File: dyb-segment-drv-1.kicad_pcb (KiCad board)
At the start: 2 copper layers, 10 x 3 mm, 183 parts, among them J1 Conn_01x10, Q1 HL2300, Q10 HL2300, Q11 HL2300, Q12 HL2300, Q13 HL2300, Q14 HL2300, Q15 HL2300, Q16 HL2300, Q2 HL2300, Q3 HL2300, Q4 HL2300, Q5 HL2300, Q6 HL2300, Q7 HL2300, Q8 HL2300, Q9 HL2300, SW1 SW_SPDT, U1 AP2112K-1.8, U10 74AUC2G32, U11 74AUC2G32, U12 74AUC2G32, U13 74AUC2G32, U14 74AUC2G32, U15 Inverter_Schmitt_Dual, U16 Inverter_Schmitt_Dual, U17 SN74AUP2G08, U18 SN74AUP2G08, U19 SN74AUP2G08, U2 GS3911AG, U20 SN74AUP2G08, U21 SN74AUP2G08, U22 74AUC2G32, U23 74AUC2G32, U24 74AUC2G32, U25 74AUC2G32, U26 74AUC2G32, U27 GS3911AG, U28 SN74AUP2G08, U29 SN74AUP2G08, U3 SN74AUP2G08, U30 SN74AUP2G08, U31 SN74AUP2G08, U32 SN74AUP2G08, U33 SN74AUP2G08, U34 74AUC2G32, U35 74AUC2G32, U36 74AUC2G32, U37 74AUC2G32, U38 74AUC2G32, U39 74AUC2G32, U4 SN74AUP2G08, U40 Inverter_Schmitt_Dual, U41 Inverter_Schmitt_Dual, U42 SN74AUP2G08, U43 SN74AUP2G08, U44 SN74AUP2G08, U45 SN74AUP2G08, U46 SN74AUP2G08, U47 74AUC2G32, U48 74AUC2G32, U49 74AUC2G32, U5 SN74AUP2G08, U50 74AUC2G32, U51 74AUC2G32, U6 SN74AUP2G08, U7 SN74AUP2G08, U8 SN74AUP2G08, U9 74AUC2G32

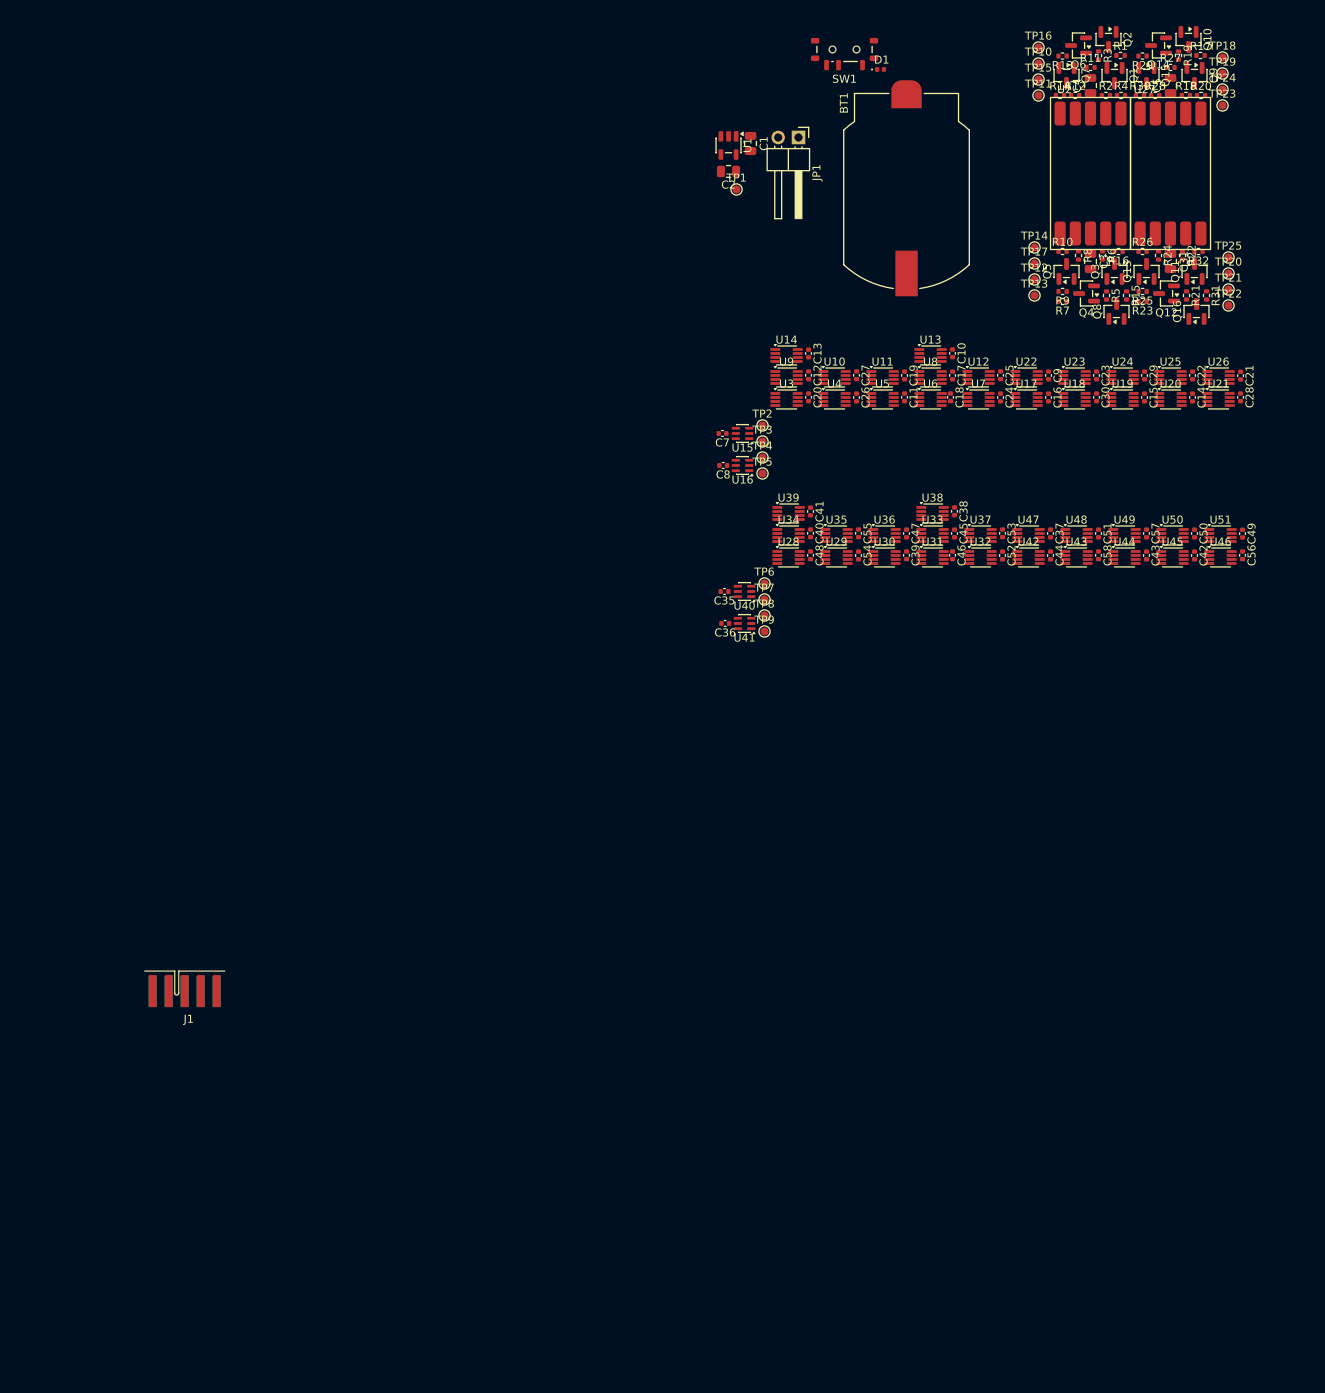
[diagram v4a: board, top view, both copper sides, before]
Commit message: pcb: add initial led driver routing
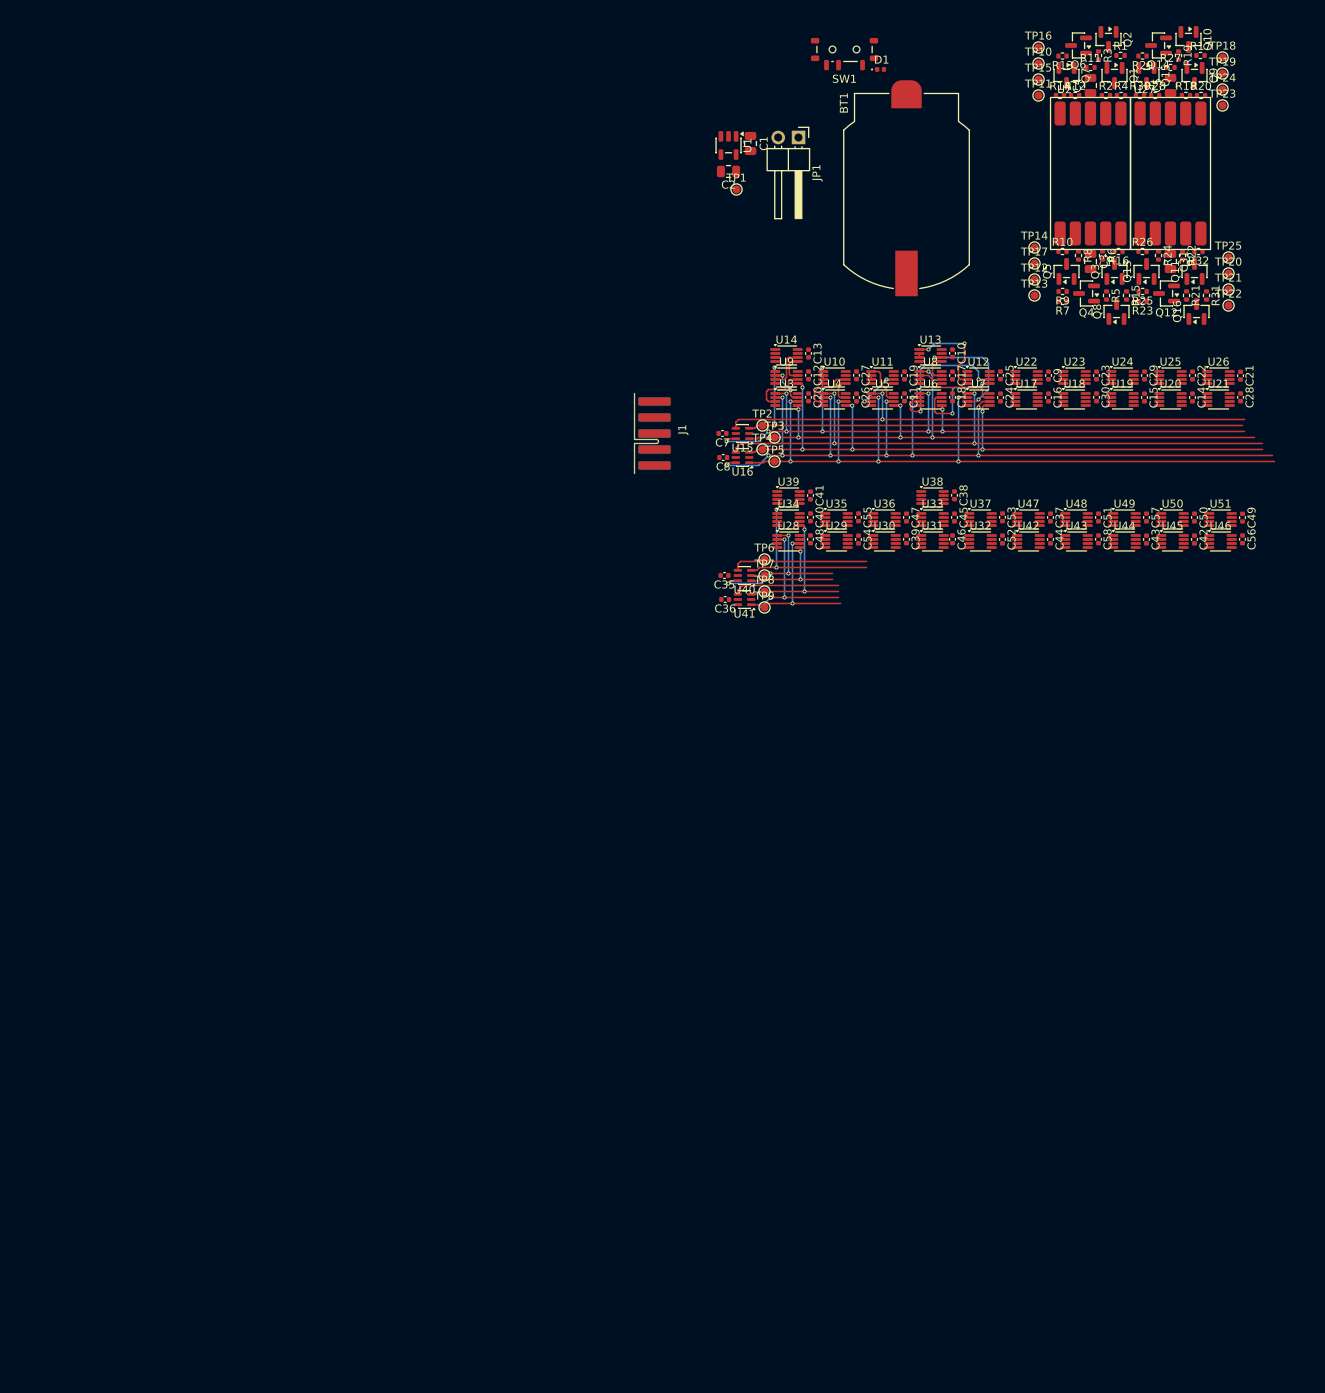
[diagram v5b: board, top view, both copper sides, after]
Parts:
- moved J1 88.1 mm to (101.8, 68.0), turned to 90 degrees
- moved C36 3.00 mm to (113.1, 91.8)
- moved TP6 3.00 mm to (118.0, 86.8)
- moved TP7 3.00 mm to (118.0, 88.8)
- moved TP8 3.00 mm to (118.0, 90.8)
- moved TP9 3.00 mm to (118.0, 92.8)
- moved U41 3.00 mm to (115.5, 91.8)
- moved TP5 2.12 mm to (119.2, 74.5)
- moved C35 2.00 mm to (113.0, 88.8)
- moved C37 2.00 mm to (153.8, 81.5)
- moved C38 2.00 mm to (141.8, 78.7)
- moved C39 2.00 mm to (135.8, 84.2)
- moved C40 2.00 mm to (123.8, 81.5)
- moved C41 2.00 mm to (123.8, 78.8)
- moved C42 2.00 mm to (171.8, 84.2)
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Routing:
- net /Segment Driver/~{D3}: track 0.00 -> 110.0 mm, vias 0 -> 12
- net /A3: track 0.00 -> 100.5 mm, vias 0 -> 8
- net /Segment Driver/~{D1}: track 0.00 -> 90.5 mm, vias 0 -> 10
- net /A2: track 0.00 -> 85.7 mm, vias 0 -> 6
- net /A1: track 0.00 -> 81.7 mm, vias 0 -> 6
- net /Segment Driver/~{D2}: track 0.00 -> 81.4 mm, vias 0 -> 4
- net /A0: track 0.00 -> 69.6 mm, vias 0 -> 2
- net /Segment Driver/~{D0}: track 0.00 -> 69.1 mm, vias 0 -> 2
- net /B0: track 0.00 -> 22.3 mm, vias 0 -> 2
- net /Segment Driver1/~{D1}: track 0.00 -> 21.0 mm, vias 0 -> 4
- net /B2: track 0.00 -> 19.8 mm, vias 0 -> 2
- net /B3: track 0.00 -> 19.6 mm, vias 0 -> 2
- net Net-(U12-Pad6): track 0.00 -> 18.7 mm, vias 0 -> 2
- net /Segment Driver1/~{D3}: track 0.00 -> 18.4 mm, vias 0 -> 3
- net /Segment Driver1/~{D0}: track 0.00 -> 17.0 mm
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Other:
- board size 10 x 3 mm -> 3 x 10 mm

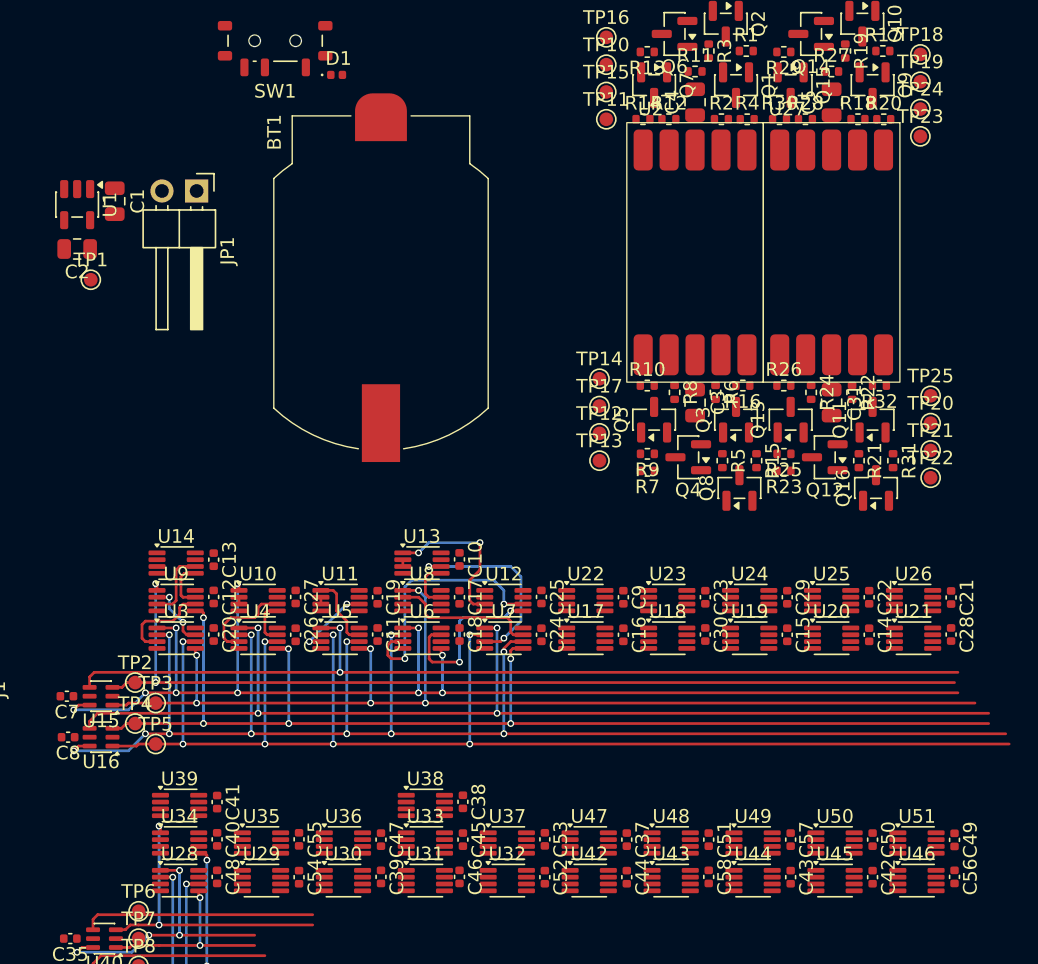
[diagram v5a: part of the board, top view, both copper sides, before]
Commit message: pcb: add tooling holes and fiducials
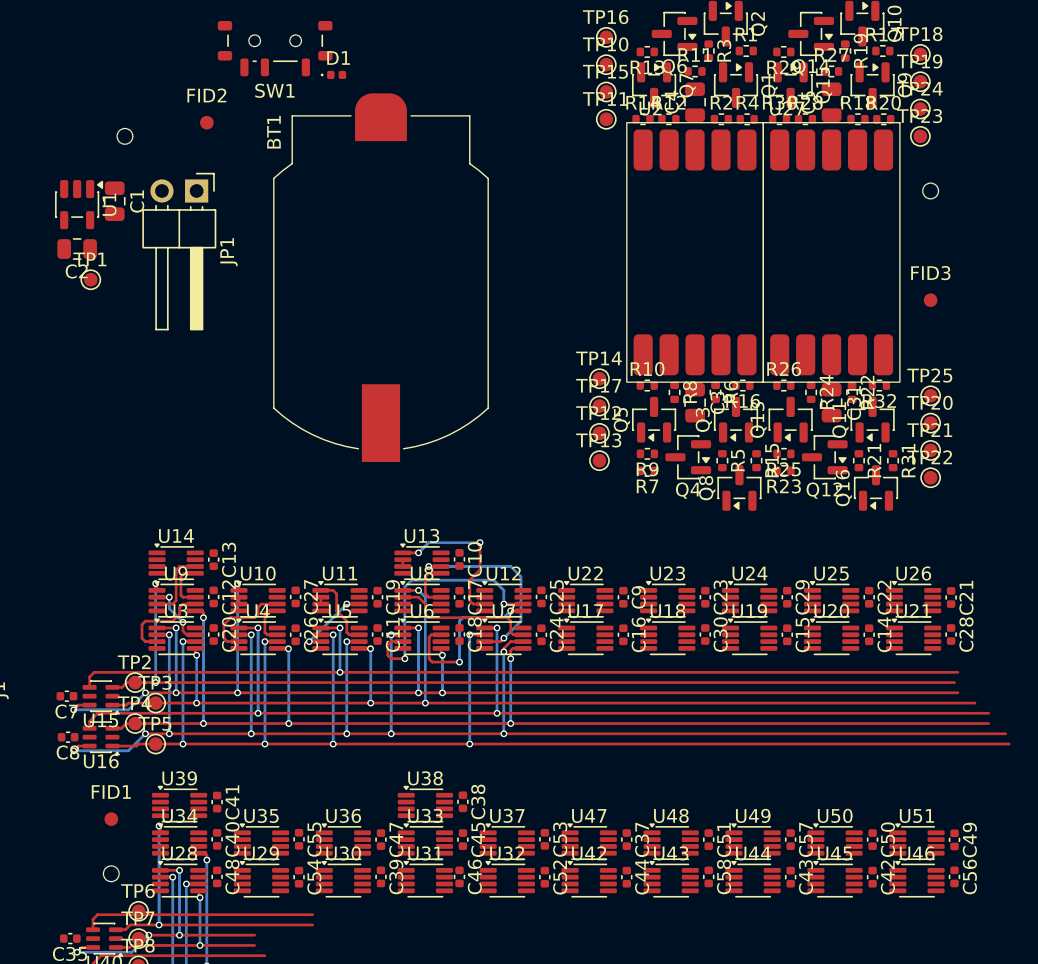
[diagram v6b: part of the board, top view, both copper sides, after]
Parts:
- added FID1: Fiducial, Fiducial:Fiducial_1mm_Mask2mm, F.Cu at (116.0, 80.0)
- added FID2: Fiducial, Fiducial:Fiducial_1mm_Mask2mm, F.Cu at (123.0, 29.0)
- added FID3: Fiducial, Fiducial:Fiducial_1mm_Mask2mm, F.Cu at (176.0, 42.0)
- added H1: MountingHole, MountingHole:ToolingHole_1.152mm, F.Cu at (116.0, 84.0)
- added H2: MountingHole, MountingHole:ToolingHole_1.152mm, F.Cu at (117.0, 30.0)
- added H3: MountingHole, MountingHole:ToolingHole_1.152mm, F.Cu at (176.0, 34.0)

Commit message: pcb: add mounting holes
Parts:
- added H4: MountingHole_Pad, MountingHole:MountingHole_3.2mm_M3_Pad_Via, F.Cu at (115.0, 24.0)
- added H5: MountingHole_Pad, MountingHole:MountingHole_3.2mm_M3_Pad_Via, F.Cu at (181.0, 90.0)
- added H6: MountingHole_Pad, MountingHole:MountingHole_3.2mm_M3_Pad_Via, F.Cu at (181.0, 24.0)

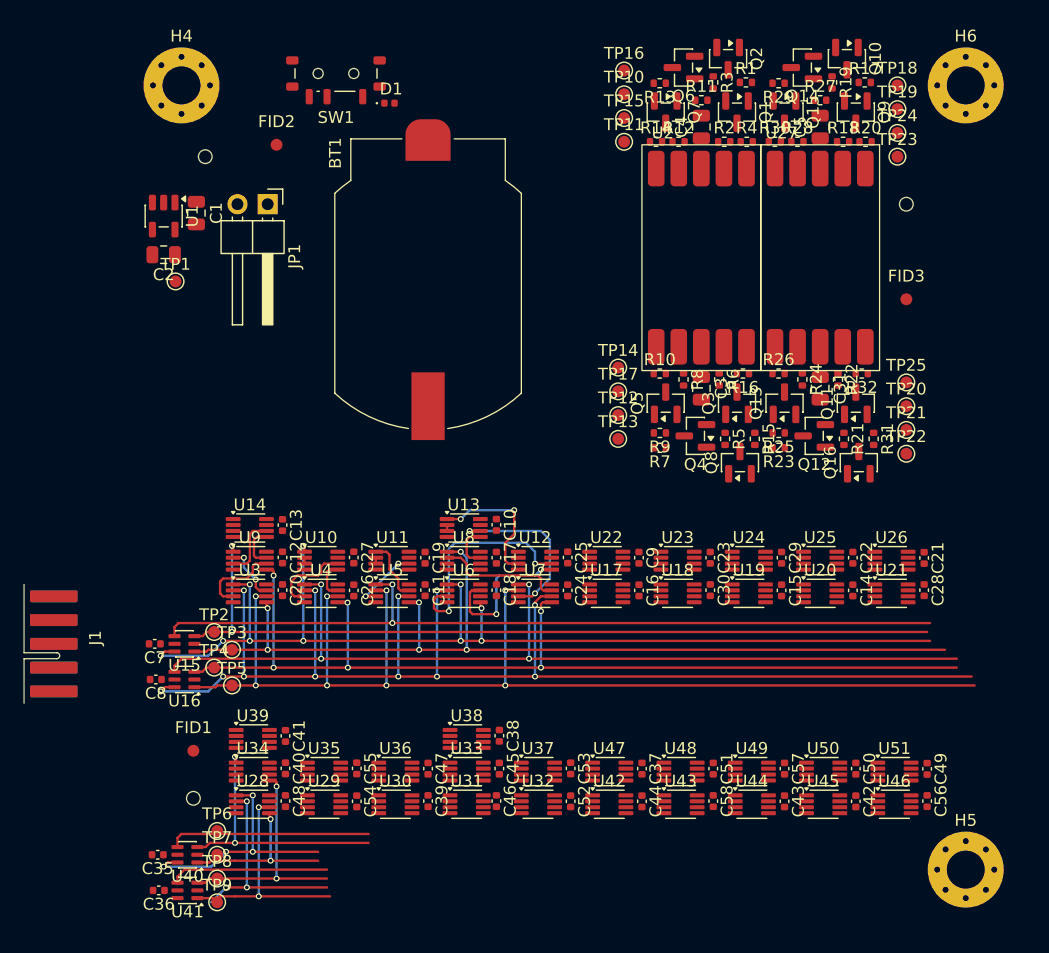
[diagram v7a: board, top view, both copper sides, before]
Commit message: pcb: add board outline
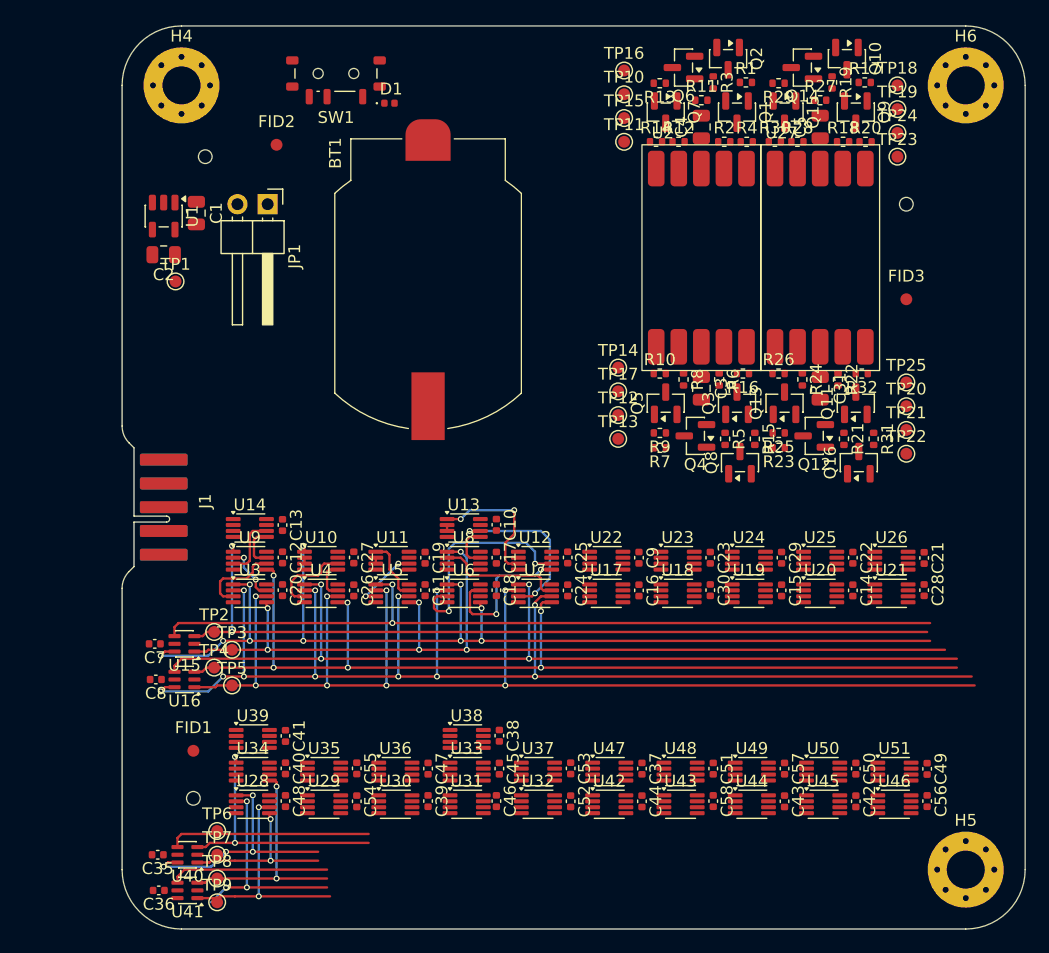
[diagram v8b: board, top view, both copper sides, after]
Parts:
- moved J1 14.8 mm to (111.0, 56.5)
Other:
- board size 3 x 10 mm -> 76 x 76 mm
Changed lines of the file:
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@@
 	(footprint "GLCS:KYOCERA_AVX9159-006"
 		(layer "F.Cu")
-		(at 101.75 68 90)
+		(at 111 56.5 90)
 		(descr "board to board 10 pin edge connector https://www.kyocera-avx.com/download/connectors/Conn-Sales-Drawings/9XXX/9159-06X.zip")
 		(tags "edge b2b")
@@
 		(embedded_fonts no)
 	)
+	(gr_arc
+		(start 110 24)
+		(mid 111.464466 20.464466)
+		(end 115 19)
+		(stroke
+			(width 0.05)
+			(type default)
+		)
+		(layer "Edge.Cuts")
+	)
+	(gr_line
+		(start 110 52.671573)
+		(end 110 24)
+		(stroke
+			(width 0.05)
+			(type default)
+		)
+		(layer "Edge.Cuts")
+	)
+	(gr_line
+		(start 110 66.328427)
+		(end 110 90)
+		(stroke
+			(width 0.05)
+			(type default)
+		)
+		(layer "Edge.Cuts")
+	)
+	(gr_arc
+		(start 110 66.328427)
+		(mid 110.152232 65.563054)
+		(end 110.585787 64.914213)
+		(stroke
+			(width 0.05)
+			(type default)
+		)
+		(layer "Edge.Cuts")
+	)
+	(gr_arc
+		(start 110.585787 54.085787)
+		(mid 110.15225 53.436939)
+		(end 110 52.671573)
+		(stroke
+			(width 0.05)
+			(type default)
+		)
+		(layer "Edge.Cuts")
+	)
+	(gr_line
+		(start 110.585787 54.085787)
+		(end 111 54.5)
+		(stroke
+			(width 0.05)
+			(type default)
+		)
+		(layer "Edge.Cuts")
+	)
+	(gr_line
+		(start 110.585787 64.914213)
+		(end 111 64.5)
+		(stroke
+			(width 0.05)
+			(type default)
+		)
+		(layer "Edge.Cuts")
+	)
+	(gr_line
+		(start 115 19)
+		(end 181 19)
+		(stroke
+			(width 0.05)
+			(type default)
+		)
+		(layer "Edge.Cuts")
+	)
+	(gr_arc
+		(start 115 95)
+		(mid 111.464466 93.535534)
+		(end 110 90)
+		(stroke
+			(width 0.05)
+			(type default)
+		)
+		(layer "Edge.Cuts")
+	)
+	(gr_arc
+		(start 181 19)
+		(mid 184.535534 20.464466)
+		(end 186 24)
+		(stroke
+			(width 0.05)
+			(type default)
+		)
+		(layer "Edge.Cuts")
+	)
+	(gr_line
+		(start 181 95)
+		(end 115 95)
+		(stroke
+			(width 0.05)
+			(type default)
+		)
+		(layer "Edge.Cuts")
+	)
+	(gr_line
+		(start 186 24)
+		(end 186 90)
+		(stroke
+			(width 0.05)
+			(type default)
+		)
+		(layer "Edge.Cuts")
+	)
+	(gr_arc
+		(start 186 90)
+		(mid 184.535534 93.535534)
+		(end 181 95)
+		(stroke
+			(width 0.05)
+			(type default)
+		)
+		(layer "Edge.Cuts")
+	)
 	(segment
